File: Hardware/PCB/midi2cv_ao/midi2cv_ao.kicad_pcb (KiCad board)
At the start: 2 copper layers, 116 x 110.5 mm, 66 parts, among them IC1 TL074, J1 Conn_01x03, J11 Conn_01x10, J12 AudioJack2, J13 AudioJack2, J14 AudioJack2, J15 AudioJack2, J16 AudioJack2, J17 AudioJack2, J18 AudioJack2, J19 AudioJack2, J2 Synth_power_2x5, J3 Conn_01x04, J4 Conn_01x04, J6 Conn_01x10

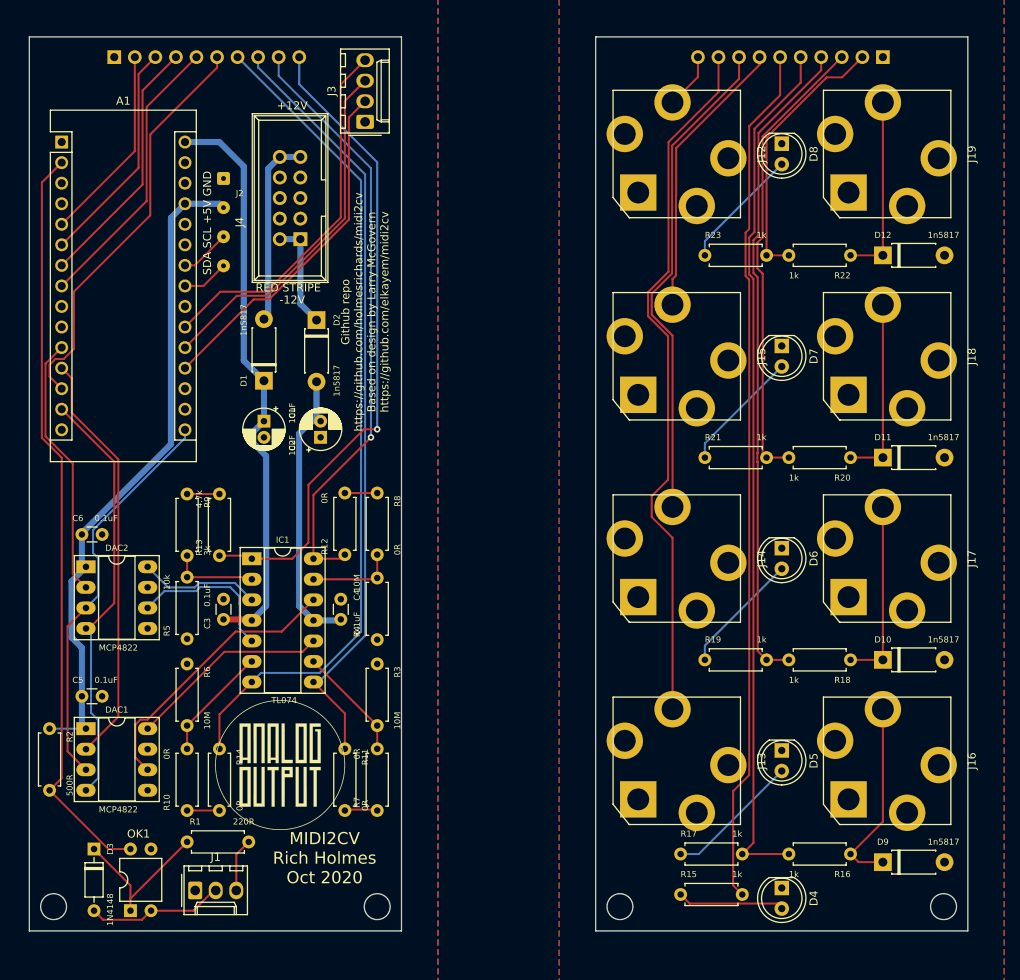
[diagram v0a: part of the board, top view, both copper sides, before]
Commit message: Revert some changes (save for a later version)
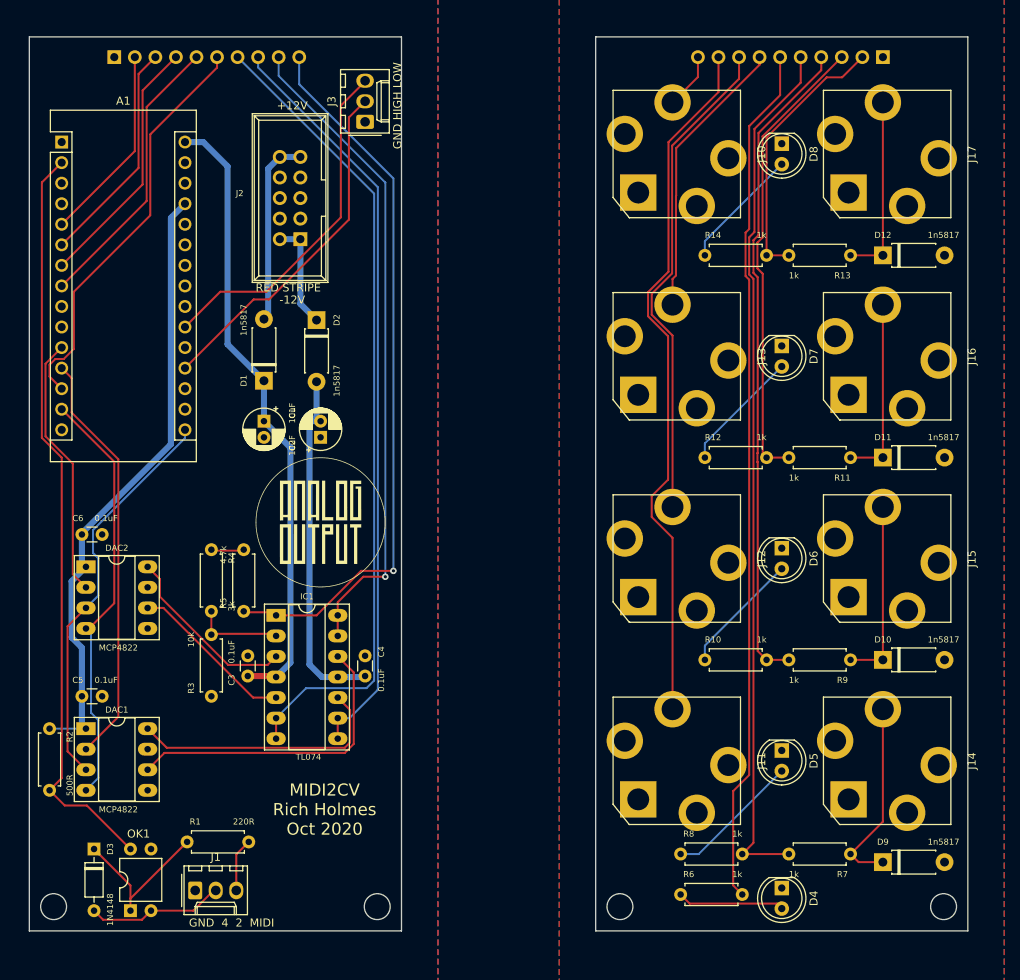
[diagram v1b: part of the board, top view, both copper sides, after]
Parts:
- removed the J4 at (64.0, 82.5)
- removed the R10 at (59.5, 160.6)
- removed the R11 at (79.0, 153.0)
- removed the R12 at (79.0, 129.0)
- removed the R13 at (63.5, 129.1)
- removed the R14 at (63.5, 153.0)
- removed the R6 at (59.5, 142.5)
- removed the R7 at (83.0, 160.6)
- removed the R8 at (83.0, 121.4)
- removed the R9 at (59.5, 121.5)
- J3: value Conn_01x04 -> Conn_01x03; footprint Connector_Molex:Molex_KK-254_AE-6410-04A_1x04_P2.54mm_Vertical -> Connector_Molex:Molex_KK-254_AE-6410-03A_1x03_P2.54mm_Vertical
- R3: value 10M -> 10k
- R4: value 10M -> 3k
- R5: value 10k -> 4.7k
- moved G*** 30.4 mm to (76.0, 125.0)
- moved R4 23.3 mm to (62.5, 128.4), turned to 270 degrees
- moved R3 20.9 mm to (62.5, 146.5), turned to 90 degrees
- moved R5 7.78 mm to (66.5, 136.0)
- moved C3 7.62 mm to (67.0, 144.0)
- moved C4 7.62 mm to (81.5, 141.5)
- moved IC1 7.62 mm to (70.5, 136.5)
- renumbered J12 to J10, J13 to J11, J14 to J12, J15 to J13, J16 to J14, J17 to J15, J18 to J16, J19 to J17, J6 to J4, J11 to J9, R19 to R10, R20 to R11, R21 to R12, R22 to R13, R23 to R14, R15 to R6, R16 to R7, R17 to R8, R18 to R9
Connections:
- A1 pad 19: /SW1 -> /SW3
- A1 pad 20: /SW2 -> Net-(A1-Pad20)
- A1 pad 21: /SW3 -> /SW1
- A1 pad 23: /SDA -> Net-(A1-Pad23)
- A1 pad 24: /SCL -> Net-(A1-Pad24)
- IC1 pad 13: Net-(IC1-Pad13) -> /CONTROL_A
- IC1 pad 6: Net-(IC1-Pad6) -> /VELOCITY_A
- IC1 pad 9: Net-(IC1-Pad9) -> /PITCH_BEND_A
- J3 pad 2: /SW1 -> /SW3
- J3 pad 3: /SW2 -> /SW1
- R3 pad 2: Net-(IC1-Pad9) -> Net-(IC1-Pad2)
- R4 pad 1: GND -> Net-(R4-Pad1)
- R4 pad 2: Net-(IC1-Pad13) -> Net-(IC1-Pad2)
- R5 pad 1: GND -> /NOTE_A
- R5 pad 2: Net-(IC1-Pad2) -> Net-(R4-Pad1)
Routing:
- net /SW2: track 44.6 -> 0.00 mm
- net Net-(IC1-Pad6): track 14.2 -> 0.00 mm
- net Net-(IC1-Pad9): track 13.9 -> 0.00 mm
- net Net-(IC1-Pad13): track 10.8 -> 0.00 mm
- net /NOTE_A: track 80.5 -> 89.3 mm
- net -12V: track 35.6 -> 44.0 mm
- net Net-(DAC2-Pad8): track 15.0 -> 22.6 mm
- net Net-(DAC1-Pad8): track 25.0 -> 32.5 mm
- net /CONTROL_A: track 73.8 -> 81.0 mm
- net /SCL: track 6.23 -> 0.00 mm
- net +12V: track 71.4 -> 77.3 mm
- net /SDA: track 5.79 -> 0.00 mm
- net +5V: track 81.3 -> 76.3 mm
- net Net-(R11-Pad2): track 4.05 -> 0.00 mm
- net Net-(R4-Pad1): track 0.00 -> 4.00 mm
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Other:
- board text added: "GATE CLK LED BEND NOTE TRIG CLK/4 VEL CC"
- board text added: "GND 4 2 MIDI"
- board text added: "GND HIGH LOW"
- board text added: "Github repo https://github.com/holmesrichards/midi2cv_ao Based on design by Larry McGovern https://github.com/elkayem/midi2cv"
- board text added: "NOTE BEND LED CLK GATE CC VEL CLK/4 TRIG"
- board text removed: "Github repo https://github.com/holmesrichards/midi2cv Based on design by Larry McGovern https://github.com/elkayem/midi2cv"
- board text removed: "SDA SCL +5V GND"

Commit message: General updates
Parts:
- J3: value Conn_01x03 -> Conn_01x06; footprint Connector_Molex:Molex_KK-254_AE-6410-03A_1x03_P2.54mm_Vertical -> Connector_Molex:Molex_KK-254_AE-6410-06A_1x06_P2.54mm_Vertical
- moved J3 26.8 mm to (55.5, 69.0), turned to 180 degrees
- moved J4 10.0 mm to (60.5, 67.5)
- moved J8 10.0 mm to (135.5, 67.5)
- renumbered D9 to D10, D10 to D11, D11 to D12, D12 to D13, D4 to D5, D5 to D6, D6 to D7, D7 to D8, D8 to D9, J11 to J10, J12 to J11, J13 to J12, J14 to J13, J15 to J14, J16 to J15, J17 to J16, J9 to J8, J10 to J9
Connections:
- A1 pad 20: Net-(A1-Pad20) -> /SW1
- A1 pad 21: /SW1 -> /BUT
- A1 pad 22: Net-(A1-Pad22) -> /PROG_LED1
- A1 pad 23: Net-(A1-Pad23) -> /PROG_LED2
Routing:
- net /BUT: track 0.00 -> 38.7 mm
- net /PROG_LED1: track 0.00 -> 35.1 mm
- net /PROG_LED2: track 0.00 -> 32.1 mm
- net /TRIGGER_A: track 28.0 -> 37.4 mm
- net /CLOCK_A: track 31.6 -> 41.0 mm
- net /GATE_A: track 24.4 -> 33.8 mm
- net /CLOCK_4_A: track 35.2 -> 44.6 mm
- net /VELOCITY_A: track 100.7 -> 91.7 mm
- net /CONTROL_A: track 81.0 -> 72.7 mm, vias 1 -> 0
- net /MIDI_LED_A: track 50.8 -> 58.3 mm
- net /NOTE_A: track 89.3 -> 82.3 mm
- net /PITCH_BEND_A: track 93.3 -> 86.8 mm
- net Net-(J8-Pad2): track 33.3 -> 28.0 mm
- net Net-(J8-Pad3): track 57.0 -> 53.1 mm
- net /Panel components/CONTROL: track 87.5 -> 90.6 mm
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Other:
- board text added: "BUT LED1-2 SW1-2 GND"
- board text added: "GATE CLK LED VEL BEND NOTE TRIG CLK/4 CC"
- board text removed: "GATE CLK LED BEND NOTE TRIG CLK/4 VEL CC"

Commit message: Add buffers to digital outputs; change optoisolator
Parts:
- removed D10, D11, D12, D13: 1n5817, ao_tht:D_DO-41_SOD81_P7.62mm_Horizontal
- removed H1, H2, H3, H4: MountingHole, ao_tht:MountingHole_3.2mm_M3
- removed OK1: SFH617A-2, Package_DIP:DIP-4_W7.62mm
- added C7: 0.1uF, ao_tht:C_Disc_D3.0mm_W1.6mm_P2.50mm, F.Cu at (77.5, 84.2)
- added C8: 0.1uF, ao_tht:C_Disc_D3.0mm_W1.6mm_P2.50mm, F.Cu at (67.0, 94.0)
- added C9: 0.1uF, ao_tht:C_Disc_D3.0mm_W1.6mm_P2.50mm, F.Cu at (46.8, 94.2)
- added D4: LED_Dual_ACA, ao_tht:TO-92_Inline_Wide, F.Cu at (268.2, 76.8)
- added IC2: TL074, ao_tht:DIP-14_W7.62mm_Socket_LongPads, F.Cu at (46.5, 75.0)
- added IC3: TL074, ao_tht:DIP-14_W7.62mm_Socket_LongPads, F.Cu at (66.5, 75.0)
- added J5: MIDIJACK, ao_tht:DIN5, F.Cu at (249.5, 85.2)
- added J6: Conn_01x03, Connector_Wire:SolderWire-0.1sqmm_1x03_P3.6mm_D0.4mm_OD1mm, F.Cu at (215.0, 145.1)
- added J7: Conn_01x06, Connector_Molex:Molex_KK-254_AE-6410-06A_1x06_P2.54mm_Vertical, F.Cu at (277.7, 86.6)
- added REF**: MountingHole_3.2mm_M3, ao_tht:MountingHole_3.2mm_M3, F.Cu at (112.5, 67.0)
- added REF**: MountingHole_3.2mm_M3, ao_tht:MountingHole_3.2mm_M3, F.Cu at (152.5, 172.0)
- added REF**: MountingHole_3.2mm_M3, ao_tht:MountingHole_3.2mm_M3, F.Cu at (83.5, 67.0)
- added REF**: MountingHole_3.2mm_M3, ao_tht:MountingHole_3.2mm_M3, F.Cu at (43.5, 172.0)
- added SW1: SW_Push, ao_tht:R_Axial_DIN0207_L6.3mm_D2.5mm_P7.62mm_Horizontal, F.Cu at (265.2, 92.2)
- added SW2: SW_SPDT, ao_tht:SPDT-toggle-switch-1M-series, F.Cu at (297.7, 74.2)
- IC1: value TL074 -> H11L1; footprint ao_tht:DIP-14_W7.62mm_Socket_LongPads -> ao_tht:DIP-6_W7.62mm_Socket_LongPads
- R2: value 500R -> 270R
- moved G*** 130.0 mm to (132.5, 104.5)
- moved A1 80.7 mm to (66.5, 155.5), turned to 180 degrees
- moved J2 78.9 mm to (69.2, 168.8), turned to 90 degrees
- moved D2 72.6 mm to (59.2, 170.8), turned to 180 degrees
- moved C4 70.8 mm to (42.8, 82.2), turned to 90 degrees
- moved C5 64.2 mm to (57.8, 83.2), turned to 90 degrees
- moved R5 61.5 mm to (77.4, 75.5), turned to 0 degrees
- moved R3 60.6 mm to (84.5, 90.0)
- moved D1 59.3 mm to (51.8, 164.2), turned to 0 degrees
- moved C2 57.6 mm to (43.5, 162.0), turned to 0 degrees
- moved J3 57.2 mm to (44.0, 125.0), turned to 270 degrees
- moved DAC1 56.5 mm to (66.5, 97.5)
- moved R4 53.8 mm to (85.0, 79.5), turned to 180 degrees
- moved D3 50.6 mm to (82.4, 128.2), turned to 180 degrees
- moved C1 49.0 mm to (45.5, 155.5), turned to 180 degrees
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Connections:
- A1 pad 5: /GATE_A -> /GATE_B
- A1 pad 6: /TRIGGER_A -> /TRIGGER_B
- A1 pad 7: /CLOCK_A -> /CLOCK_B
- A1 pad 8: /CLOCK_4_A -> /CLOCK_4_B
- C3 pad 1: +12V -> GND
- C3 pad 2: GND -> +5V
- C4 pad 1: GND -> +12V
- C4 pad 2: -12V -> GND
- C5 pad 1: +5V -> GND
- C5 pad 2: GND -> -12V
- C6 pad 1: +5V -> +12V
- IC1 pad 1: /NOTE_A -> Net-(D3-Pad1)
- IC1 pad 2: Net-(IC1-Pad2) -> /MIDI4
- IC1 pad 3: Net-(DAC2-Pad8) -> Net-(IC1-Pad3)
- IC1 pad 4: +12V -> /RX0
- IC1 pad 5: Net-(DAC2-Pad6) -> GND
- IC1 pad 6: /VELOCITY_A -> +5V
- J3 pad 4: /PROG_LED2 -> /BUT
- J3 pad 6: /BUT -> /PROG_LED2
- R3 pad 2: Net-(IC1-Pad2) -> Net-(IC3-Pad13)
- R4 pad 2: Net-(IC1-Pad2) -> Net-(IC3-Pad13)
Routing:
- net -12V: track 43.4 -> 161.4 mm, vias 0 -> 2
- net /VELOCITY_A: track 91.7 -> 10.8 mm
- net /CLOCK_4_B: track 0.00 -> 75.0 mm, vias 0 -> 2
- net /GATE_B: track 0.00 -> 73.8 mm, vias 0 -> 1
- net /RX0: track 93.2 -> 20.3 mm
- net /CLOCK_B: track 0.00 -> 71.5 mm, vias 0 -> 1
- net /TRIGGER_B: track 0.00 -> 68.2 mm, vias 0 -> 2
- net /NOTE_A: track 82.3 -> 16.6 mm, vias 1 -> 0
- net +5V: track 76.3 -> 140.7 mm, vias 0 -> 1
- net /PITCH_BEND_A: track 86.8 -> 24.0 mm
- net +12V: track 76.1 -> 127.3 mm, vias 0 -> 2
- net /CONTROL_A: track 72.7 -> 24.2 mm
- net /SW3: track 40.8 -> 7.27 mm
- net /SW1: track 40.0 -> 7.27 mm
- net /BUT: track 38.7 -> 7.27 mm
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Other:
- board size 116 x 110.5 mm -> 115 x 111 mm
- net class PWR added: clearance 0.2, trace_width 0.75, via_dia 0.8, via_drill 0.4
- board text added: "MIDI 2 4 GND"
- board text added: "MIDI2CV Rich Holmes / Jan 2021"
- board text removed: "BUT LED1-2 SW1-2 GND"
- board text removed: "GND 4 2 MIDI"
- board text removed: "GND HIGH LOW"
- board text removed: "MIDI2CV Rich Holmes Oct 2020"

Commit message: Jumper for hard/soft serial select
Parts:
- removed the G*** at (132.5, 104.5)
- added J17: Conn_01x03, Connector_PinHeader_2.54mm:PinHeader_1x03_P2.54mm_Vertical, F.Cu at (70.8, 149.8)
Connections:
- A1 pad 10: Net-(A1-Pad10) -> /SOFT_RX
- IC1 pad 4: /RX0 -> /RX_J
- R2 pad 2: /RX0 -> /RX_J
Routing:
- net /RX_J: track 0.00 -> 20.6 mm
- net /RX0: track 20.3 -> 5.56 mm
- net /SOFT_RX: track 0.00 -> 13.8 mm
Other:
- board text added: "HARD SERIAL"
- board text added: "SOFT SERIAL"

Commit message: Include lib table files; backlogged changes
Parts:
- added G***: LOGO, midi2cv_ao:midi2cv_ao_panel_holes, F.Cu at (132.5, 107.0)
- added REF**: MountingHole_3.2mm_M3, ao_tht:MountingHole_3.2mm_M3, F.Cu at (152.5, 67.0)
- added REF**: MountingHole_3.2mm_M3, ao_tht:MountingHole_3.2mm_M3, F.Cu at (112.5, 172.0)
- added REF**: MountingHole_3.2mm_M3, ao_tht:MountingHole_3.2mm_M3, F.Cu at (43.5, 67.0)
- added REF**: MountingHole_3.2mm_M3, ao_tht:MountingHole_3.2mm_M3, F.Cu at (83.5, 172.0)
- A1: footprint Module:Arduino_Nano -> ao_tht:Arduino_Nano
- D4: footprint ao_tht:TO-92_Inline_Wide -> ao_tht:LED_D5.0mm-3
- J6: footprint Connector_Wire:SolderWire-0.1sqmm_1x03_P3.6mm_D0.4mm_OD1mm -> ao_tht:Molex_KK-254_AE-6410-03A_1x03_P2.54mm_Vertical
- SW1: footprint ao_tht:R_Axial_DIN0207_L6.3mm_D2.5mm_P7.62mm_Horizontal -> ao_tht:Push_button_A-5050
- moved J7 212.8 mm to (100.5, 204.4)
- moved SW2 212.8 mm to (120.5, 192.0), turned to 90 degrees
- moved D4 212.8 mm to (91.0, 194.6)
- moved J5 212.8 mm to (72.3, 203.1)
- moved SW1 203.4 mm to (106.0, 218.8)
- moved J6 157.5 mm to (74.8, 216.8), turned to 180 degrees
- moved D2 17.2 mm to (43.0, 165.2), turned to 90 degrees
- moved C1 10.0 mm to (45.0, 145.5)
- moved J2 9.76 mm to (59.5, 169.2)
- moved C2 9.75 mm to (43.2, 152.2)
- moved D1 8.00 mm to (47.2, 157.6), turned to 270 degrees
- moved G*** 2.10 mm to (77.2, 115.0), turned to 0 degrees
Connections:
- D4 pad 2: Net-(D4-Pad2) -> GND2
- J5 pad 3: Net-(J5-Pad3) -> GND2
- J6 pad 1: Net-(J5-Pad3) -> GND2
- J7 pad 1: Net-(D4-Pad2) -> GND2
- SW1 pad 1: Net-(D4-Pad2) -> GND2
- SW2 pad 2: Net-(D4-Pad2) -> GND2
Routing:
- net GND2: track 0.00 -> 94.4 mm
- net Net-(J7-Pad3): track 0.00 -> 24.8 mm
- net Net-(D4-Pad1): track 0.00 -> 21.2 mm
- net Net-(D4-Pad3): track 0.00 -> 18.6 mm
- net Net-(J7-Pad2): track 0.00 -> 17.9 mm
- net Net-(J7-Pad6): track 0.00 -> 16.6 mm
- net Net-(J5-Pad2): track 0.00 -> 15.8 mm
- net Net-(J5-Pad4): track 0.00 -> 13.3 mm
- net +12V: track 127.3 -> 118.2 mm
- net Net-(D2-Pad1): track 13.4 -> 20.4 mm
- net -12V: track 161.4 -> 155.6 mm
- net Net-(D1-Pad2): track 23.4 -> 26.8 mm
- net Net-(J8-Pad2): track 54.8 -> 52.1 mm
- net /Panel components/GATE: track 30.8 -> 28.2 mm
- net +5V: track 140.7 -> 141.9 mm
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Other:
- outline, holes or cut-outs redrawn

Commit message: New routing
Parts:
- removed D4: LED_Dual_ACA, ao_tht:LED_D5.0mm-3
- removed G***: LOGO, ao_tht:analogoutput
- removed J5: MIDIJACK, ao_tht:DIN5
- removed J6: Conn_01x03, ao_tht:Molex_KK-254_AE-6410-03A_1x03_P2.54mm_Vertical
- removed J7: Conn_01x06, Connector_Molex:Molex_KK-254_AE-6410-06A_1x06_P2.54mm_Vertical
- removed REF** (x8): MountingHole_3.2mm_M3, ao_tht:MountingHole_3.2mm_M3
- removed SW1: SW_Push, ao_tht:Push_button_A-5050
- removed SW2: SW_SPDT, ao_tht:SPDT-toggle-switch-1M-series
- added G***1: LOGO, ao_tht:analogoutput_12mm, F.Cu at (74.5, 118.0)
- added REF**1: MountingHole_3.2mm_M3, ao_tht:MountingHole_3.2mm_M3, F.Cu at (42.5, 67.0)
- added REF**2: MountingHole_3.2mm_M3, ao_tht:MountingHole_3.2mm_M3, F.Cu at (82.5, 67.0)
- added REF**3: MountingHole_3.2mm_M3, ao_tht:MountingHole_3.2mm_M3, F.Cu at (42.5, 172.0)
- added REF**4: MountingHole_3.2mm_M3, ao_tht:MountingHole_3.2mm_M3, F.Cu at (82.5, 172.0)
- added REF**5: MountingHole_3.2mm_M3, ao_tht:MountingHole_3.2mm_M3, F.Cu at (122.5, 67.0)
- added REF**6: MountingHole_3.2mm_M3, ao_tht:MountingHole_3.2mm_M3, F.Cu at (162.5, 67.0)
- added REF**7: MountingHole_3.2mm_M3, ao_tht:MountingHole_3.2mm_M3, F.Cu at (122.5, 172.0)
- added REF**8: MountingHole_3.2mm_M3, ao_tht:MountingHole_3.2mm_M3, F.Cu at (162.5, 172.0)
- moved D5 10.00 mm to (141.2, 171.5)
- moved D6 10.00 mm to (142.5, 153.2)
- moved D7 10.00 mm to (142.5, 128.2)
- moved D8 10.00 mm to (142.5, 103.2)
- moved D9 10.00 mm to (142.5, 78.2)
- moved J10 10.00 mm to (129.5, 154.5)
- moved J11 10.00 mm to (129.5, 129.5)
- moved J12 10.00 mm to (129.5, 104.5)
- moved J13 10.00 mm to (155.5, 154.5)
- moved J14 10.00 mm to (155.5, 129.5)
- moved J15 10.00 mm to (155.5, 104.5)
- moved J16 10.00 mm to (155.5, 79.5)
- moved J8 10.00 mm to (153.0, 67.5)
- moved J9 10.00 mm to (129.5, 79.5)
- moved R10 10.00 mm to (133.0, 142.0)
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- renumbered G*** to G***1
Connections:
- D5 pad 1: GND1 -> (no net)
- D5 pad 2: Net-(D5-Pad2) -> (no net)
- D6 pad 1: GND1 -> (no net)
- D6 pad 2: Net-(D6-Pad2) -> (no net)
- D7 pad 1: GND1 -> (no net)
- D7 pad 2: Net-(D7-Pad2) -> (no net)
- D8 pad 1: GND1 -> (no net)
- D8 pad 2: Net-(D8-Pad2) -> (no net)
- D9 pad 1: GND1 -> (no net)
- D9 pad 2: Net-(D9-Pad2) -> (no net)
- J10 pad S: GND1 -> (no net)
- J10 pad T: /Panel components/CONTROL -> (no net)
- J11 pad S: GND1 -> (no net)
- J11 pad T: /Panel components/PITCH_BEND -> (no net)
- J12 pad S: GND1 -> (no net)
- J12 pad T: /Panel components/VELOCITY -> (no net)
- J13 pad S: GND1 -> (no net)
- J13 pad T: /Panel components/CLOCK_4 -> (no net)
- J14 pad S: GND1 -> (no net)
- J14 pad T: /Panel components/CLOCK -> (no net)
- J15 pad S: GND1 -> (no net)
- J15 pad T: /Panel components/TRIGGER -> (no net)
- J16 pad S: GND1 -> (no net)
- J16 pad T: /Panel components/GATE -> (no net)
- J8 pad 1: GND1 -> (no net)
- J8 pad 10: /Panel components/NOTE -> (no net)
- J8 pad 2: Net-(J8-Pad2) -> (no net)
- J8 pad 3: Net-(J8-Pad3) -> (no net)
- J8 pad 4: Net-(J8-Pad4) -> (no net)
- J8 pad 5: Net-(J8-Pad5) -> (no net)
- J8 pad 6: Net-(J8-Pad6) -> (no net)
- J8 pad 7: /Panel components/VELOCITY -> (no net)
- J8 pad 8: /Panel components/PITCH_BEND -> (no net)
- J8 pad 9: /Panel components/CONTROL -> (no net)
- J9 pad S: GND1 -> (no net)
- J9 pad T: /Panel components/NOTE -> (no net)
- R10 pad 1: Net-(D7-Pad2) -> (no net)
- R10 pad 2: Net-(J8-Pad4) -> (no net)
- R11 pad 1: /Panel components/TRIGGER -> (no net)
- R11 pad 2: Net-(J8-Pad3) -> (no net)
- R12 pad 1: Net-(D8-Pad2) -> (no net)
- R12 pad 2: Net-(J8-Pad3) -> (no net)
- R13 pad 1: /Panel components/GATE -> (no net)
- R13 pad 2: Net-(J8-Pad2) -> (no net)
- R14 pad 1: Net-(D9-Pad2) -> (no net)
- R14 pad 2: Net-(J8-Pad2) -> (no net)
- R6 pad 1: Net-(D5-Pad2) -> (no net)
- R6 pad 2: Net-(J8-Pad6) -> (no net)
- R7 pad 1: /Panel components/CLOCK_4 -> (no net)
- R7 pad 2: Net-(J8-Pad5) -> (no net)
- R8 pad 1: Net-(D6-Pad2) -> (no net)
- R8 pad 2: Net-(J8-Pad5) -> (no net)
- R9 pad 1: /Panel components/CLOCK -> (no net)
- R9 pad 2: Net-(J8-Pad4) -> (no net)
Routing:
- net (no net): track 0.00 -> 725.3 mm
- net Net-(J8-Pad6): track 105.5 -> 0.00 mm
- net Net-(J8-Pad5): track 105.4 -> 0.00 mm
- net GND2: track 94.4 -> 0.00 mm
- net /Panel components/CONTROL: track 93.1 -> 0.00 mm
- net Net-(J8-Pad4): track 79.7 -> 0.00 mm, vias 1 -> 0
- net Net-(J8-Pad3): track 64.8 -> 0.00 mm, vias 1 -> 0
- net /Panel components/PITCH_BEND: track 60.3 -> 0.00 mm
- net Net-(J8-Pad2): track 52.1 -> 0.00 mm, vias 1 -> 0
- net -12V: track 155.6 -> 116.7 mm, vias 2 -> 0
- net /Panel components/TRIGGER: track 35.0 -> 0.00 mm
- net /Panel components/VELOCITY: track 34.2 -> 0.00 mm
- net /Panel components/GATE: track 28.2 -> 0.00 mm, vias 1 -> 0
- net Net-(J7-Pad3): track 24.8 -> 0.00 mm
- net Net-(D4-Pad1): track 21.2 -> 0.00 mm
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- added copper zone on B.Cu, net (none)
- added copper zone on F.Cu, net (none)
- removed copper zone on B.Cu, net GND1
- removed copper zone on F.Cu, net GND1
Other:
- board size 115 x 111 mm -> 126 x 111 mm
